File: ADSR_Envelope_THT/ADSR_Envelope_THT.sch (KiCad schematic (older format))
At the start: 51 parts, among them J1 AudioJack1_Switch, J2 AudioJack1_Switch, J3 Conn_02x08_Odd_Even, J4 AudioJack1_Switch, Q1 2N7000, Q2 2N3904, Q3 2N3904, Q4 2N3904, SW1 SW_Push, SW2 SW_DPDT_x2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

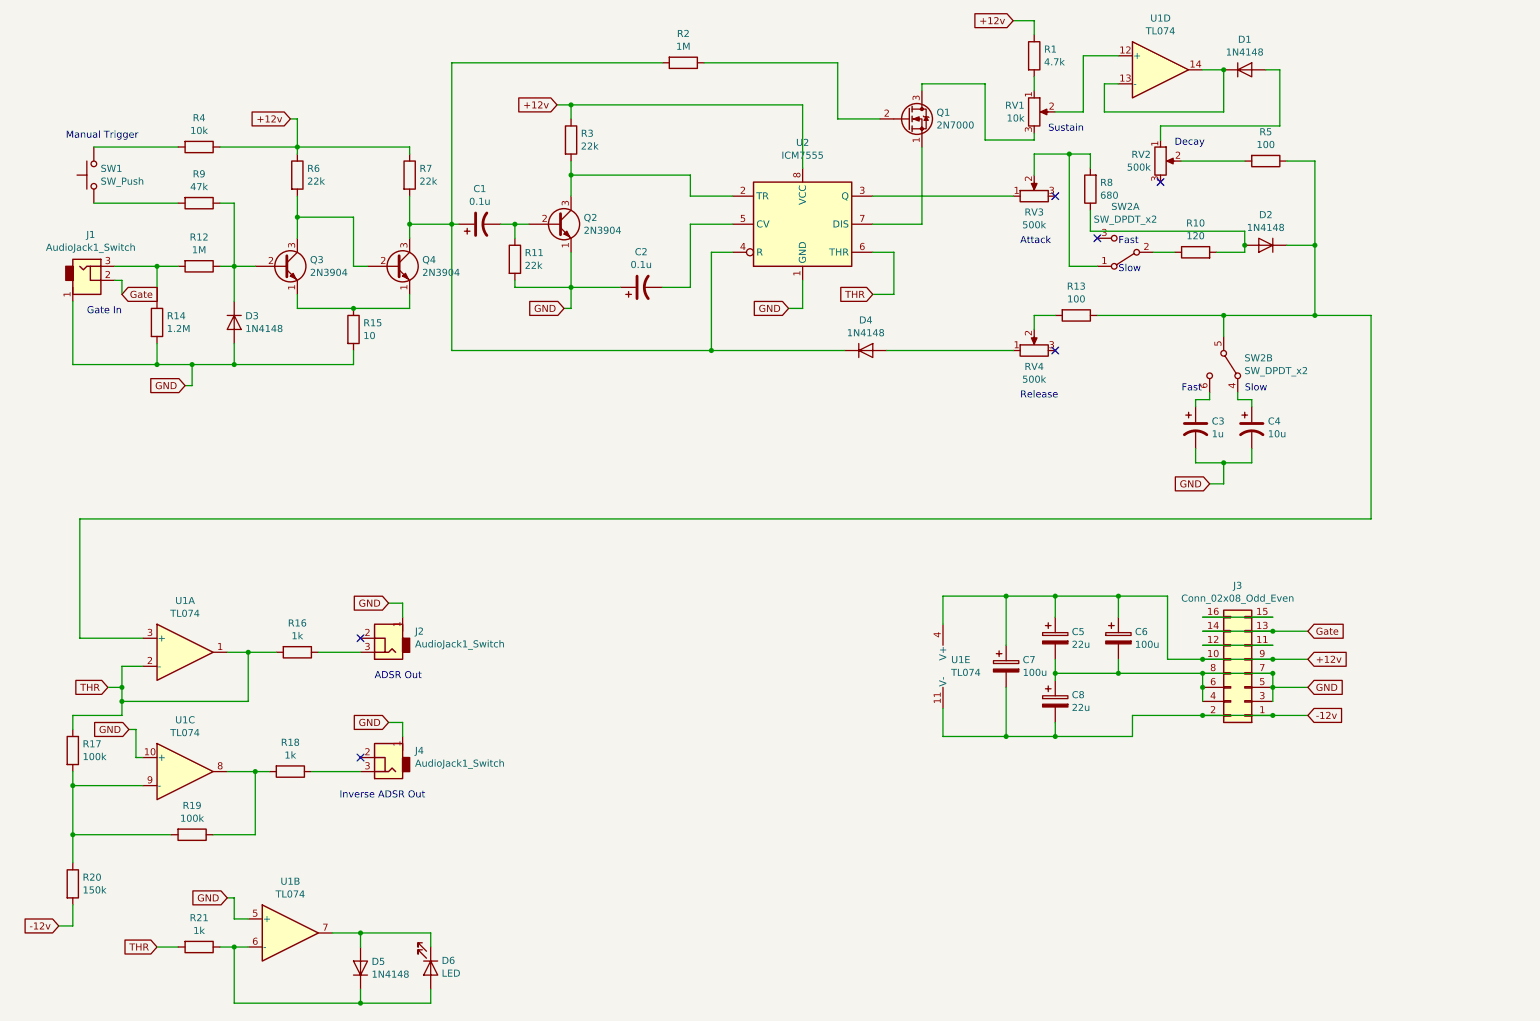
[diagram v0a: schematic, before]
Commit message: ADSR Envelope
Updated the Schematic for the ADSR Envilope and started on the PCB layout
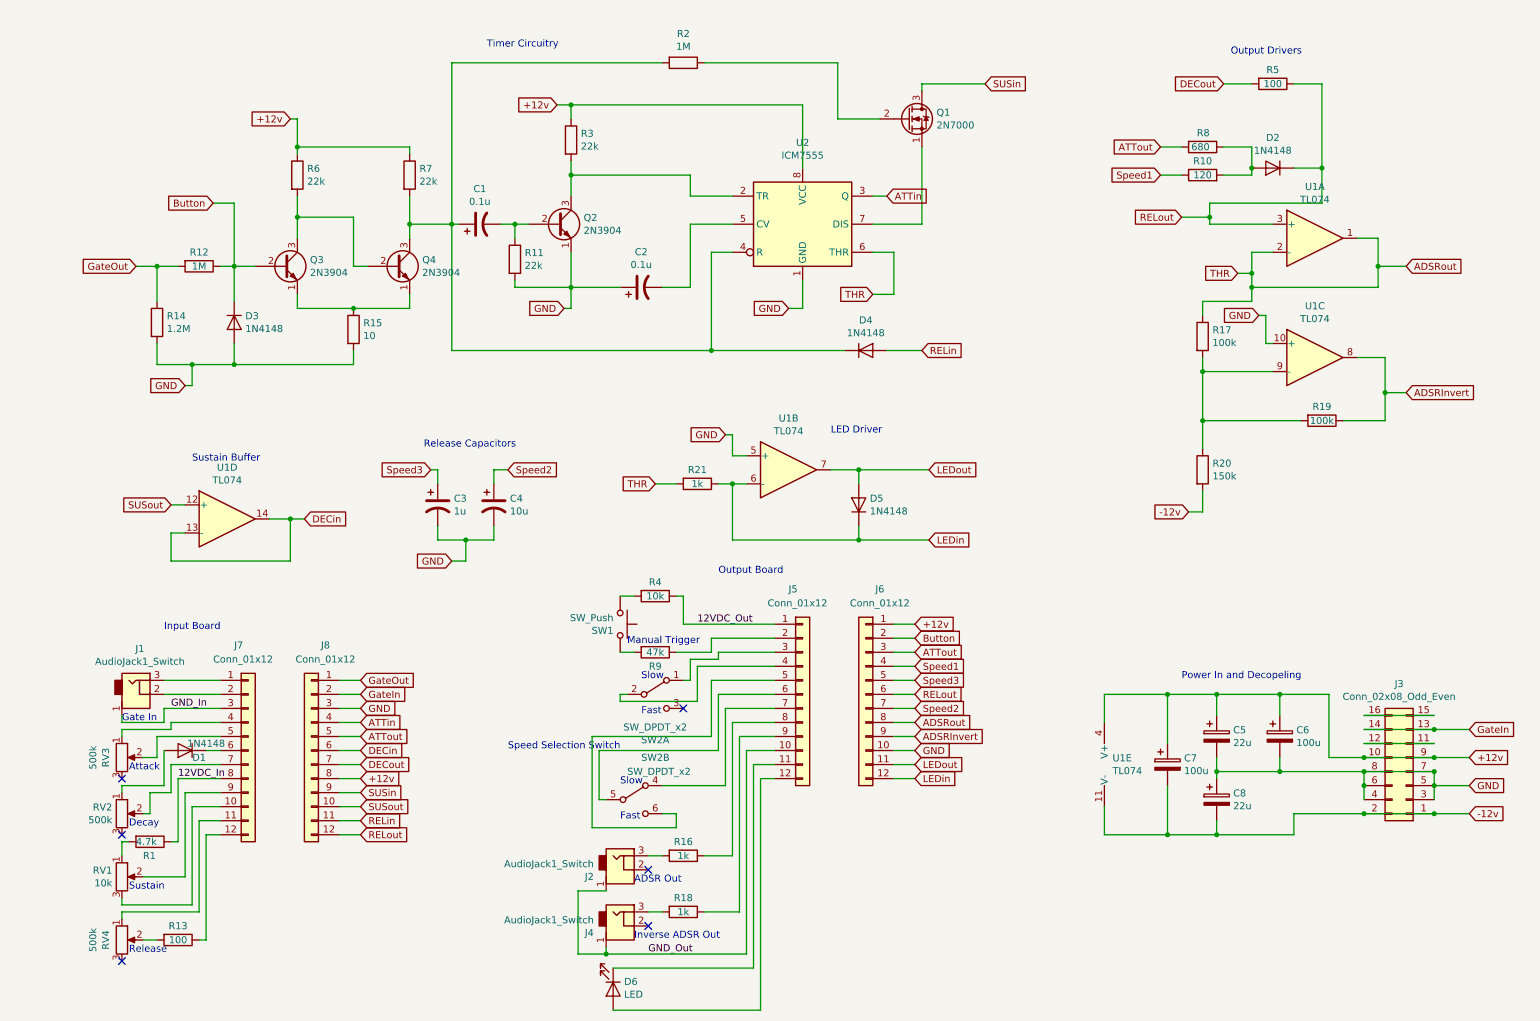
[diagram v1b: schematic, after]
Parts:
- added J5, J6, J7, J8: Conn_01x12, Pin_Headers:Pin_Header_Straight_1x12_Pitch2.54mm, symbol Connector_Generic:Conn_01x12
- SW1: footprint SamacSys_Parts:FSMRACDAH -> Custom_Library:SW_Tactile_TE_FSMRACDAH
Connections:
- net +12v: now also J6.1 (Pin_1), J8.8 (Pin_8); no longer R1.1, R4.1
- net GND: now also J6.10 (Pin_10), J8.3 (Pin_3); no longer J1.1, J2.1, J4.1
- net Button: now reaches D3.1 (K), Q3.2 (B), R12.1
- net Button: now also J6.2 (Pin_2); no longer R9.1
- net GateOut: now reaches R12.2, R14.1
- net GateOut: now also J8.1 (Pin_1); no longer J1.3
- net at R9.2: now also SW1.2; no longer SW1.1
- net at R4.2: now also SW1.1; no longer SW1.2
- net at RV3.1: now also J7.4 (Pin_4); no longer U2.3 (Q)
- net at RV4.1: now also J7.11 (Pin_11); no longer D4.2 (A)
- net at RV1.3: now also J7.10 (Pin_10); no longer Q1.3 (D)
- net at RV1.2: now also J7.9 (Pin_9); no longer U1.12 (+)
- net at RV2.2: now also J7.7 (Pin_7); no longer R5.2
- net DECin: now reaches U1.13 (-), U1.14
- net DECin: now also J8.6 (Pin_6); no longer D1.1 (K)
- net at SW2.2 (B): now also J5.4 (Pin_4); no longer R10.1
- net at SW2.4 (A): now also J5.7 (Pin_7); no longer C4.1
- net RELout: now reaches D2.1 (K), R5.1, U1.3 (+)
- net RELout: now also J6.6 (Pin_6), J8.12 (Pin_12); no longer R13.1, SW2.5 (B)
- net at SW2.6 (C): now also J5.5 (Pin_5); no longer C3.1
- net LEDin: now reaches D5.1 (K), R21.1, U1.6 (-)
- net LEDin: now also J6.12 (Pin_12); no longer D6.2 (A)
- net LEDout: now reaches D5.2 (A), U1.7
- net LEDout: now also J6.11 (Pin_11); no longer D6.1 (K)
- net ADSRInvert: now reaches R19.1, U1.8
- net ADSRInvert: now also J6.9 (Pin_9); no longer R18.2
- net at R18.1: now also J5.9 (Pin_9); no longer J4.3
- net at J2.3: now also R16.2; no longer R16.1
- net Gate renamed GateIn
- net GateIn: now also J8.2 (Pin_2); no longer J1.2
- net THR renamed ADSRout
- net ADSRout: now also J6.8 (Pin_8); no longer R16.2
- new net: J1.2, J7.2 (Pin_2)
- new net: J1.3, J7.1 (Pin_1)
- new net: J5.2 (Pin_2), R9.1
- new net: J7.5 (Pin_5), RV3.2
- new net: D1.1 (K), J7.6 (Pin_6)
- new net: J5.3 (Pin_3), SW2.1 (A)
- new net: J5.6 (Pin_6), SW2.5 (B)
- new net: J7.12 (Pin_12), R13.1
- new net: J4.3, R18.2
- new net: J5.8 (Pin_8), R16.1
- new net: D6.1 (K), J5.11 (Pin_11)
- new net: D6.2 (A), J5.12 (Pin_12)
- new net 12VDC_In: J7.8 (Pin_8), R1.1
- new net 12VDC_Out: J5.1 (Pin_1), R4.1
- new net ATTin: J8.4 (Pin_4), U2.3 (Q)
- new net ATTout: J6.3 (Pin_3), J8.5 (Pin_5), R8.2
- new net DECout: J8.7 (Pin_7), R5.2
- new net GND_In: J1.1, J7.3 (Pin_3)
- new net GND_Out: J2.1, J4.1, J5.10 (Pin_10)
- new net RELin: D4.2 (A), J8.11 (Pin_11)
- new net SUSin: J8.9 (Pin_9), Q1.3 (D)
- new net SUSout: J8.10 (Pin_10), U1.12 (+)
- new net Speed1: J6.4 (Pin_4), R10.1
- new net Speed2: C4.1, J6.7 (Pin_7)
- new net Speed3: C3.1, J6.5 (Pin_5)
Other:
- note added: "Input Board"
- note added: "LED Driver"
- note added: "Output Board\n"
- note added: "Output Drivers\n"
- note added: "Power In and Decopeling\n"
- note added: "Release Capacitors"
- note added: "Speed Selection Switch"
- note added: "Sustain Buffer\n"
- note added: "Timer Circuitry"
- moved on the sheet: C3, C4, C5, C6, C7, C8, D1, D2, D5, D6, J1, J2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

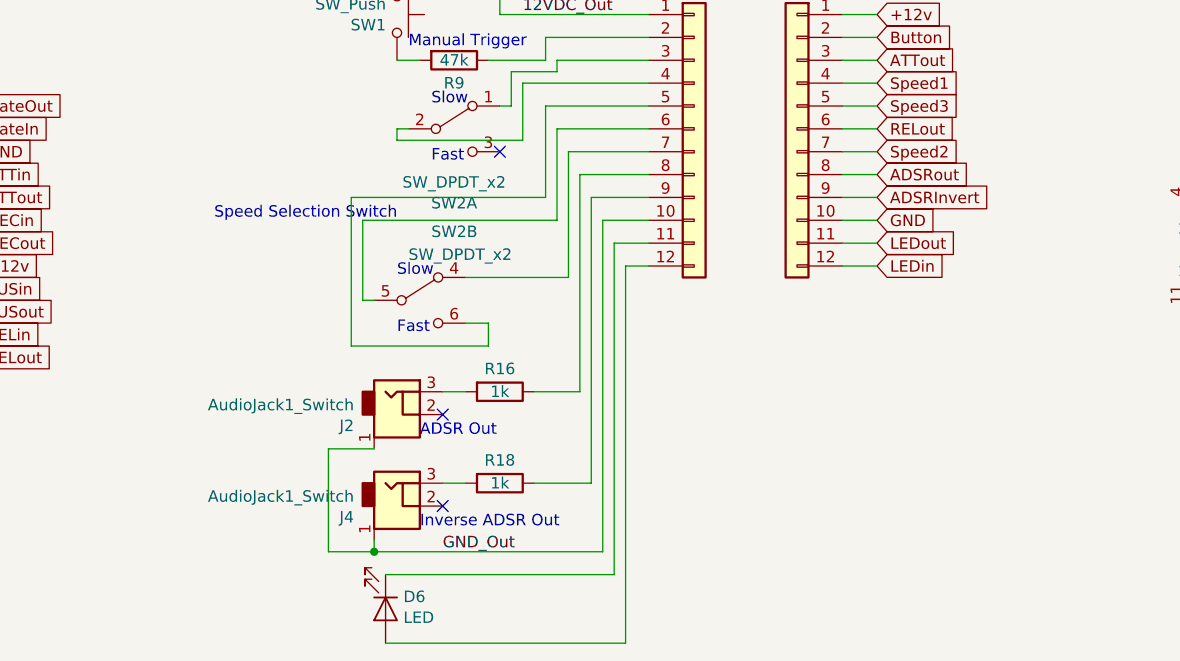
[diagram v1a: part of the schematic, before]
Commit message: ADSR Envelope
Finished the PCB design on the ADSR Envelope
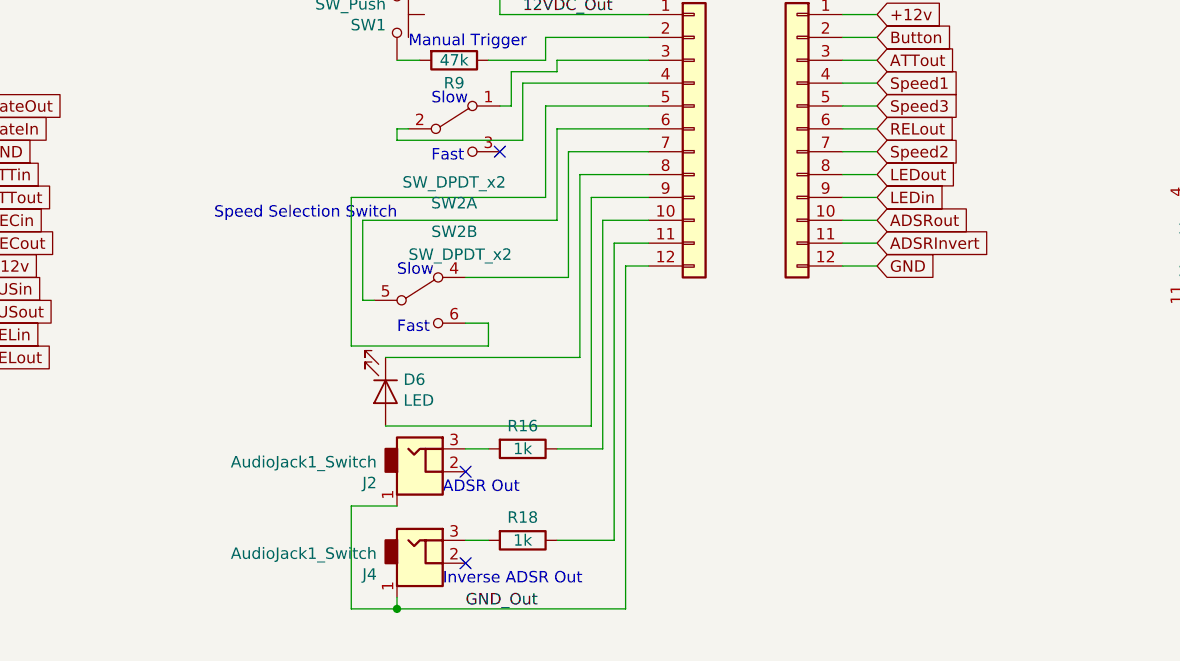
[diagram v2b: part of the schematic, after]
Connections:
- net ADSRInvert: now also J6.11 (Pin_11); no longer J6.9 (Pin_9)
- net ADSRout: now also J6.10 (Pin_10); no longer J6.8 (Pin_8)
- net GND: now also J6.12 (Pin_12); no longer J6.10 (Pin_10)
- net GND_Out: now also J5.12 (Pin_12); no longer J5.10 (Pin_10)
- net LEDin: now also J6.9 (Pin_9); no longer J6.12 (Pin_12)
- net LEDout: now also J6.8 (Pin_8); no longer J6.11 (Pin_11)
- net at R18.1: now also J5.11 (Pin_11); no longer J5.9 (Pin_9)
- net at R16.1: now also J5.10 (Pin_10); no longer J5.8 (Pin_8)
- net at D6.1 (K): now also J5.8 (Pin_8); no longer J5.11 (Pin_11)
- net at D6.2 (A): now also J5.9 (Pin_9); no longer J5.12 (Pin_12)
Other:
- moved on the sheet: D6, J2, J4, R16, R18
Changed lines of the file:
@@
 L Device:R R18
 U 1 1 5F46B0D6
-P 5250 6950
-F 0 "R18" V 5150 6950 50  0000 C CNN
-F 1 "1k" V 5250 6950 50  0000 C CNN
-F 2 "Resistors_THT:R_Axial_DIN0207_L6.3mm_D2.5mm_P10.16mm_Horizontal" V 5180 6950 50  0001 C CNN
-F 3 "~" H 5250 6950 50  0001 C CNN
-	1    5250 6950
+P 5350 7200
+F 0 "R18" V 5250 7200 50  0000 C CNN
+F 1 "1k" V 5350 7200 50  0000 C CNN
+F 2 "Resistors_THT:R_Axial_DIN0207_L6.3mm_D2.5mm_P10.16mm_Horizontal" V 5280 7200 50  0001 C CNN
+F 3 "~" H 5350 7200 50  0001 C CNN
+	1    5350 7200
 	0    1    1    0
 $EndComp
@@
 L Custom_Lib:AudioJack1_Switch J2
 U 1 1 5F471B9C
-P 4800 6650
-F 0 "J2" H 4612 6601 50  0000 R CNN
-F 1 "AudioJack1_Switch" H 4612 6692 50  0000 R CNN
-F 2 "Custom_Library:Mono_Jack_3.5mm_Switch_Switchcraft_35RAPC2AH3" H 4800 6650 50  0001 C CNN
-F 3 "~" H 4800 6650 50  0001 C CNN
-	1    4800 6650
+P 4900 6900
+F 0 "J2" H 4712 6851 50  0000 R CNN
+F 1 "AudioJack1_Switch" H 4712 6942 50  0000 R CNN
+F 2 "Custom_Library:Mono_Jack_3.5mm_Switch_Switchcraft_35RAPC2AH3" H 4900 6900 50  0001 C CNN
+F 3 "~" H 4900 6900 50  0001 C CNN
+	1    4900 6900
 	1    0    0    -1
 $EndComp
@@
 L Device:R R16
 U 1 1 5F4731BC
-P 5250 6550
-F 0 "R16" V 5150 6550 50  0000 C CNN
-F 1 "1k" V 5250 6550 50  0000 C CNN
-F 2 "Resistors_THT:R_Axial_DIN0207_L6.3mm_D2.5mm_P10.16mm_Horizontal" V 5180 6550 50  0001 C CNN
-F 3 "~" H 5250 6550 50  0001 C CNN
-	1    5250 6550
+P 5350 6800
+F 0 "R16" V 5250 6800 50  0000 C CNN
+F 1 "1k" V 5350 6800 50  0000 C CNN
+F 2 "Resistors_THT:R_Axial_DIN0207_L6.3mm_D2.5mm_P10.16mm_Horizontal" V 5280 6800 50  0001 C CNN
+F 3 "~" H 5350 6800 50  0001 C CNN
+	1    5350 6800
 	0    1    1    0
 $EndComp
-NoConn ~ 5000 6650
+NoConn ~ 5100 6900
 $Comp
 L Custom_Lib:AudioJack1_Switch J4
 U 1 1 5F487430
-P 4800 7050
-F 0 "J4" H 4612 7001 50  0000 R CNN
-F 1 "AudioJack1_Switch" H 4612 7092 50  0000 R CNN
-F 2 "Custom_Library:Mono_Jack_3.5mm_Switch_Switchcraft_35RAPC2AH3" H 4800 7050 50  0001 C CNN
-F 3 "~" H 4800 7050 50  0001 C CNN
-	1    4800 7050
-	1    0    0    -1
-$EndComp
-NoConn ~ 5000 7050
+P 4900 7300
+F 0 "J4" H 4712 7251 50  0000 R CNN
+F 1 "AudioJack1_Switch" H 4712 7342 50  0000 R CNN
+F 2 "Custom_Library:Mono_Jack_3.5mm_Switch_Switchcraft_35RAPC2AH3" H 4900 7300 50  0001 C CNN
+F 3 "~" H 4900 7300 50  0001 C CNN
+	1    4900 7300
+	1    0    0    -1
+$EndComp
+NoConn ~ 5100 7300
 Text Notes 1250 5600 0    50   ~ 0
 Gate In
 Text Notes 4850 5050 0    50   ~ 0
 Manual Trigger
-Text Notes 4900 6750 0    50   ~ 0
+Text Notes 5000 7000 0    50   ~ 0
 ADSR Out
-Text Notes 4900 7150 0    50   ~ 0
+Text Notes 5000 7400 0    50   ~ 0
 Inverse ADSR Out
-Text GLabel 6900 5800 2    50   Input ~ 0
+Text GLabel 6900 6000 2    50   Input ~ 0
 GND
 Wire Wire Line
@@
 L Device:LED D6
 U 1 1 5F4F93D6
-P 4750 7500
-F 0 "D6" V 4697 7578 50  0000 L CNN
-F 1 "LED" V 4788 7578 50  0000 L CNN
-F 2 "LEDs:LED_Rectangular_W3.9mm_H1.9mm" H 4750 7500 50  0001 C CNN
-F 3 "~" H 4750 7500 50  0001 C CNN
-	1    4750 7500
+P 4750 6550
+F 0 "D6" V 4697 6628 50  0000 L CNN
+F 1 "LED" V 4788 6628 50  0000 L CNN
+F 2 "LEDs:LED_Rectangular_W3.9mm_H1.9mm" H 4750 6550 50  0001 C CNN
+F 3 "~" H 4750 6550 50  0001 C CNN
+	1    4750 6550
 	0    1    1    0
 $EndComp
@@
 	4800 4700 4900 4700
 Wire Wire Line
-	5100 6550 5000 6550
-Wire Wire Line
-	5100 6950 5000 6950
+	5200 6800 5100 6800
+Wire Wire Line
+	5200 7200 5100 7200
 Text GLabel 10400 2350 2    50   Input ~ 0
 ADSRout
-Text GLabel 6900 5700 2    50   Input ~ 0
+Text GLabel 6900 5900 2    50   Input ~ 0
 ADSRInvert
 Wire Wire Line
@@
 Wire Wire Line
 	10200 2350 10200 2150
-Text GLabel 6900 5600 2    50   Input ~ 0
+Text GLabel 6900 5800 2    50   Input ~ 0
 ADSRout
 Text GLabel 10400 3250 2    50   Input ~ 0
@@
 Text GLabel 7000 4300 2    50   Input ~ 0
 LEDin
-Text GLabel 6900 6000 2    50   Input ~ 0
+Text GLabel 6900 5700 2    50   Input ~ 0
 LEDin
-Text GLabel 6900 5900 2    50   Input ~ 0
+Text GLabel 6900 5600 2    50   Input ~ 0
 LEDout
 Wire Wire Line
-	4750 7350 5750 7350
+	4750 6400 5600 6400
 Wire Wire Line
 	5750 5900 5900 5900
@@
 	5900 5800 5700 5800
 Wire Wire Line
-	5700 7250 4700 7250
-Wire Wire Line
-	4700 7250 4700 7200
-Wire Wire Line
-	4700 6800 4500 6800
-Wire Wire Line
-	4500 6800 4500 7250
-Wire Wire Line
-	4500 7250 4700 7250
-Connection ~ 4700 7250
-Wire Wire Line
-	5400 6550 5600 6550
+	5800 7500 4800 7500
+Wire Wire Line
+	4800 7500 4800 7450
+Wire Wire Line
+	4800 7050 4600 7050
+Wire Wire Line
+	4600 7050 4600 7500
+Wire Wire Line
+	4600 7500 4800 7500
+Connection ~ 4800 7500
+Wire Wire Line
+	5500 6800 5700 6800
 Wire Wire Line
 	5600 5600 5900 5600
@@
 Wire Wire Line
 	3500 3800 3500 3900
-Wire Wire Line
-	5600 5600 5600 6550
-Wire Wire Line
-	5700 5800 5700 7250
-Wire Wire Line
-	5750 5900 5750 7350
 Text Notes 5500 4550 0    50   ~ 0
 Output Board\n
@@
 	4650 5800 4650 6150
 Wire Wire Line
-	5400 6950 5650 6950
+	5500 7200 5750 7200
 Wire Wire Line
 	5650 5700 5900 5700
 Wire Wire Line
-	5650 5700 5650 6950
-Wire Wire Line
 	5900 6000 5800 6000
-Wire Wire Line
-	5800 6000 5800 7650
-Wire Wire Line
-	5800 7650 4750 7650
 Wire Wire Line
 	5900 5500 5550 5500
@@
 Text Label 5350 4900 0    50   ~ 0
 12VDC_Out
-Text Label 5000 7250 0    50   ~ 0
+Text Label 5100 7500 0    50   ~ 0
 GND_Out
 Text Label 1650 6000 0    50   ~ 0
@@
 Text Label 1600 5500 0    50   ~ 0
 GND_In
+Wire Wire Line
+	5600 5600 5600 6400
+Wire Wire Line
+	5650 5700 5650 6700
+Wire Wire Line
+	5650 6700 4750 6700
+Wire Wire Line
+	5700 5800 5700 6800
+Wire Wire Line
+	5750 5900 5750 7200
+Wire Wire Line
+	5800 6000 5800 7500
 $EndSCHEMATC
